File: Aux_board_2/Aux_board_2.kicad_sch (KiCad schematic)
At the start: 72 parts, among them J1 P10d, J2 R_ENC, J3 Z_ENC, J4 Z_LIM_UP, J5 Z_LIM_DN, J6 Z_HOME, Q1 BSS138, Q10 BSS84, Q11 BSS138, Q12 BSS84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

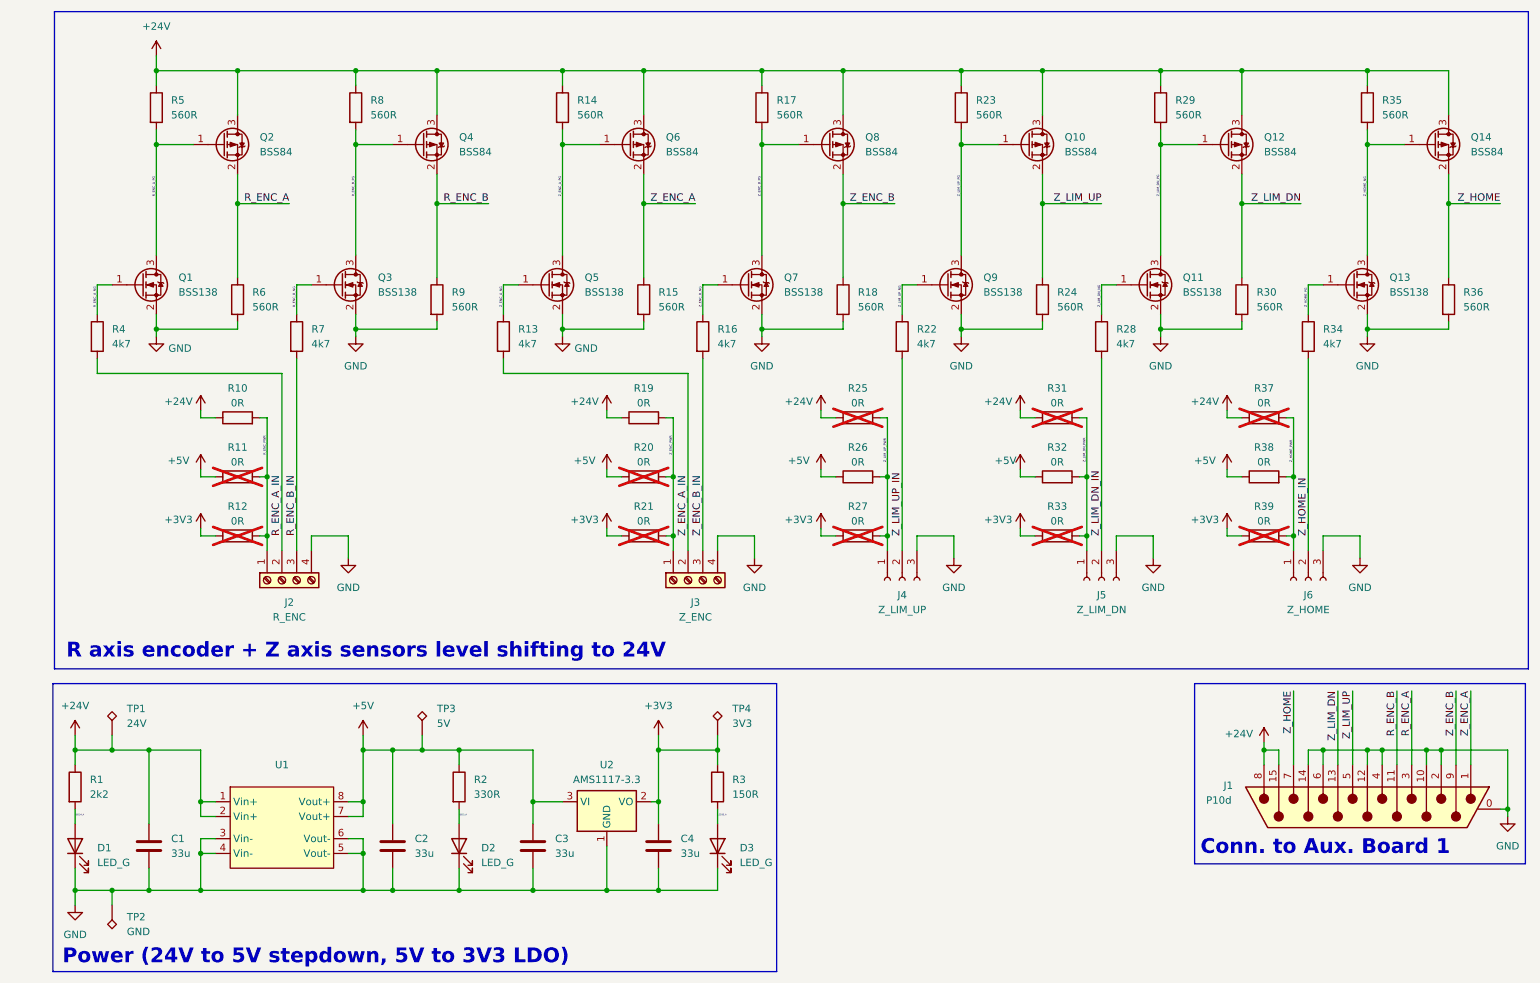
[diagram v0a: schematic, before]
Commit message: Started placement&routing Board 2
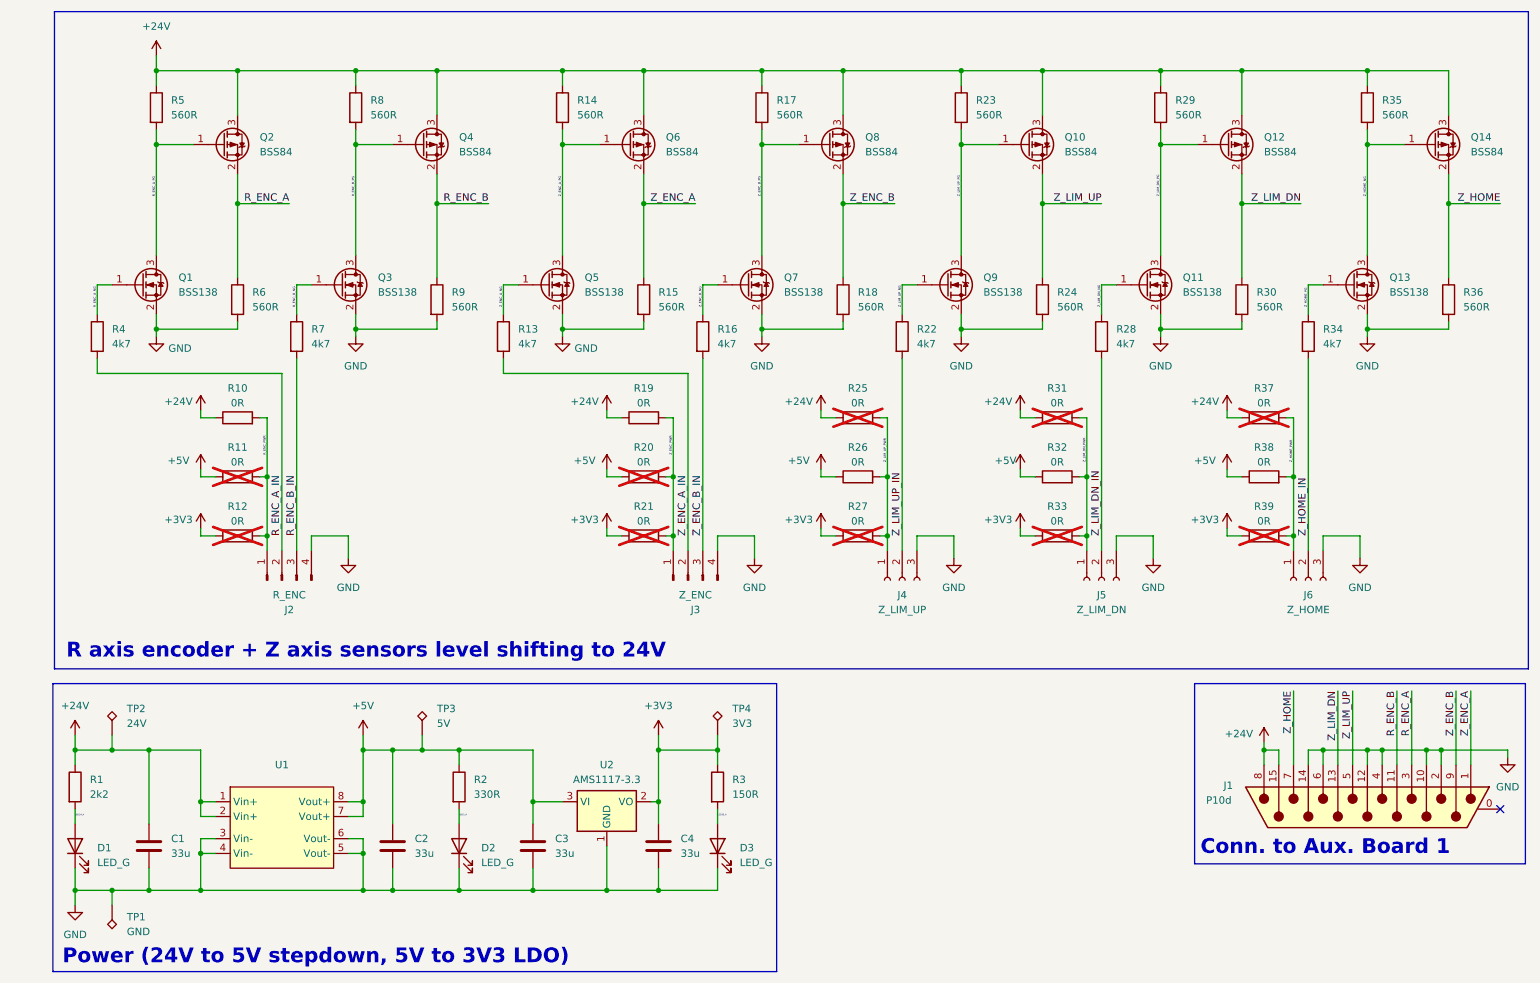
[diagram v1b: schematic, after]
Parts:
- J1: footprint (none) -> Connector_Dsub:DSUB-15_Male_Horizontal_P2.77x2.84mm_EdgePinOffset7.70mm_Housed_MountingHolesOffset9.12mm
- J2, J3: footprint TerminalBlock_4Ucon:TerminalBlock_4Ucon_1x04_P3.50mm_Horizontal -> Connector_PinHeader_2.54mm:PinHeader_1x04_P2.54mm_Horizontal; symbol Connector:Screw_Terminal_01x04 -> Connector:Conn_01x04_Pin
- J4, J5, J6: footprint Connector_PinSocket_2.54mm:PinSocket_1x03_P2.54mm_Vertical -> Connector_PinHeader_2.54mm:PinHeader_1x03_P2.54mm_Horizontal
- renumbered TP2 to TP1, TP1 to TP2
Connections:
- net GND: no longer J1.0 (PAD)
- no-connect marks 0 -> 1
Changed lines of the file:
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@@
 	)
 	(junction
-		(at 270.51 153.67)
-		(diameter 0)
-		(color 0 0 0 0)
-	)
-	(junction
 		(at 156.21 49.53)
 		(diameter 0)
@@
 		(color 0 0 0 0)
 	)
+	(no_connect
+		(at 269.24 153.67)
+	)
 	(wire
 		(pts
@@
 	(wire
 		(pts
-			(xy 269.24 153.67) (xy 270.51 153.67)
-		)
-		(stroke
-			(width 0)
-			(type default)
-		)
-	)
-	(wire
-		(pts
 			(xy 264.16 133.35) (xy 264.16 146.05)
 		)
@@
 	(wire
 		(pts
-			(xy 270.51 154.94) (xy 270.51 153.67)
-		)
-		(stroke
-			(width 0)
-			(type default)
-		)
-	)
-	(wire
-		(pts
 			(xy 62.23 76.2) (xy 62.23 109.22)
 		)
@@
 	(wire
 		(pts
-			(xy 270.51 143.51) (xy 270.51 153.67)
+			(xy 270.51 143.51) (xy 270.51 144.78)
 		)
 		(stroke
@@
 	)
 	(symbol
-		(lib_id "Connector:Screw_Terminal_01x04")
+		(lib_id "Connector:Conn_01x04_Pin")
 		(at 59.69 114.3 90)
-		(mirror x)
 		(unit 1)
 		(exclude_from_sim no)
@@
 		(on_board yes)
 		(dnp no)
-		(fields_autoplaced yes)
 		(property "Reference" "J2"
-			(at 60.96 118.11 90)
+			(at 60.96 119.38 90)
 			(effects
 				(font
@@
 		)
 		(property "Value" "R_ENC"
-			(at 60.96 120.65 90)
+			(at 60.96 116.84 90)
 			(effects
 				(font
@@
 			)
 		)
-		(property "Footprint" "TerminalBlock_4Ucon:TerminalBlock_4Ucon_1x04_P3.50mm_Horizontal"
+		(property "Footprint" "Connector_PinHeader_2.54mm:PinHeader_1x04_P2.54mm_Horizontal"
 			(at 59.69 114.3 0)
 			(effects
@@
 			)
 		)
-		(property "Description" "Generic screw terminal, single row, 01x04, script generated (kicad-library-utils/schlib/autogen/connector/)"
+		(property "Description" "Generic connector, single row, 01x04, script generated"
 			(at 59.69 114.3 0)
 			(effects
@@
 			)
 		)
-		(property "Footprint" "Connector_PinSocket_2.54mm:PinSocket_1x03_P2.54mm_Vertical"
+		(property "Footprint" "Connector_PinHeader_2.54mm:PinHeader_1x03_P2.54mm_Horizontal"
 			(at 200.66 114.3 0)
 			(effects
@@
 		(dnp no)
 		(fields_autoplaced yes)
-		(property "Reference" "TP2"
+		(property "Reference" "TP1"
 			(at 33.02 172.2119 0)
 			(effects
@@
 			(project "Aux_board_2"
 				(path "/ff8e15cb-437c-4c01-afcb-c2153cdf3814"
-					(reference "TP2")
+					(reference "TP1")
 					(unit 1)
 				)
@@
 			)
 		)
-		(property "Footprint" "Connector_PinSocket_2.54mm:PinSocket_1x03_P2.54mm_Vertical"
+		(property "Footprint" "Connector_PinHeader_2.54mm:PinHeader_1x03_P2.54mm_Horizontal"
 			(at 166.37 114.3 0)
 			(effects
@@
 	(symbol
 		(lib_id "power:GND")
-		(at 270.51 154.94 0)
+		(at 270.51 144.78 0)
 		(mirror y)
 		(unit 1)
@@
 		(fields_autoplaced yes)
 		(property "Reference" "#PWR01"
-			(at 270.51 161.29 0)
+			(at 270.51 151.13 0)
 			(effects
 				(font
@@
 		)
 		(property "Value" "GND"
-			(at 270.51 160.02 0)
+			(at 270.51 149.86 0)
 			(effects
 				(font
@@
 		)
 		(property "Footprint" ""
-			(at 270.51 154.94 0)
+			(at 270.51 144.78 0)
 			(effects
 				(font
@@
 		)
 		(property "Datasheet" ""
-			(at 270.51 154.94 0)
+			(at 270.51 144.78 0)
 			(effects
 				(font
@@
 		)
 		(property "Description" "Power symbol creates a global label with name \"GND\" , ground"
-			(at 270.51 154.94 0)
+			(at 270.51 144.78 0)
 			(effects
 				(font
@@
 			)
 		)
-		(property "Footprint" ""
+		(property "Footprint" "Connector_Dsub:DSUB-15_Male_Horizontal_P2.77x2.84mm_EdgePinOffset7.70mm_Housed_MountingHolesOffset9.12mm"
 			(at 246.38 153.67 0)
 			(effects
@@
 		(dnp no)
 		(fields_autoplaced yes)
-		(property "Reference" "TP1"
+		(property "Reference" "TP2"
 			(at 33.02 136.3979 0)
 			(effects
@@
 			(project "Aux_board_2"
 				(path "/ff8e15cb-437c-4c01-afcb-c2153cdf3814"
-					(reference "TP1")
+					(reference "TP2")
 					(unit 1)
 				)
@@
 	)
 	(symbol
-		(lib_id "Connector:Screw_Terminal_01x04")
+		(lib_id "Connector:Conn_01x04_Pin")
 		(at 129.54 114.3 90)
-		(mirror x)
 		(unit 1)
 		(exclude_from_sim no)
@@
 		(on_board yes)
 		(dnp no)
-		(fields_autoplaced yes)
 		(property "Reference" "J3"
-			(at 130.81 118.11 90)
+			(at 130.81 119.38 90)
 			(effects
 				(font
@@
 		)
 		(property "Value" "Z_ENC"
-			(at 130.81 120.65 90)
+			(at 130.81 116.84 90)
 			(effects
 				(font
@@
 			)
 		)
-		(property "Footprint" "TerminalBlock_4Ucon:TerminalBlock_4Ucon_1x04_P3.50mm_Horizontal"
+		(property "Footprint" "Connector_PinHeader_2.54mm:PinHeader_1x04_P2.54mm_Horizontal"
 			(at 129.54 114.3 0)
 			(effects
@@
 			)
 		)
-		(property "Description" "Generic screw terminal, single row, 01x04, script generated (kicad-library-utils/schlib/autogen/connector/)"
+		(property "Description" "Generic connector, single row, 01x04, script generated"
 			(at 129.54 114.3 0)
 			(effects
@@
 			)
 		)
-		(property "Footprint" "Connector_PinSocket_2.54mm:PinSocket_1x03_P2.54mm_Vertical"
+		(property "Footprint" "Connector_PinHeader_2.54mm:PinHeader_1x03_P2.54mm_Horizontal"
 			(at 236.22 114.3 0)
 			(effects
